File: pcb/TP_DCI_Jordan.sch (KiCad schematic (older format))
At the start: 20 parts

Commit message: Rótulo en esquemático
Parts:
- added JP?: +Led, Connector_PinHeader_2.54mm:PinHeader_1x02_P2.54mm_Vertical, symbol Jumper:Jumper_2_Open
- J?: symbol PCB_LCD-rescue:Conn_01x16_Male-copia-miConector -> TP_DCI_Jordan-rescue:Conn_01x16_Male-copia-miConector-PCB_LCD-rescue
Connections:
- wire segments 73 -> 77
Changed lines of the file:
@@
 EESchema Schematic File Version 4
-LIBS:PCB_LCD-cache
+LIBS:TP_DCI_Jordan-cache
 EELAYER 29 0
 EELAYER END
@@
 encoding utf-8
 Sheet 1 1
-Title ""
-Date ""
-Rev ""
+Title "Adaptador LCD-i2c para Displays Alfanuméricos"
+Date "2022-07-03"
+Rev "1.0"
 Comp ""
-Comment1 ""
-Comment2 ""
-Comment3 ""
-Comment4 ""
+Comment1 "Autor: Jordán Joan Emmanuel"
+Comment2 "Materia:  Diseño de Circuitos Impresos"
+Comment3 "Carrera de Especialización en Sistemas Embebidos"
+Comment4 "Facultad de Ingeniería de la Universidad de Buenos Aires"
 $EndDescr
 $Comp
@@
 $EndComp
 $Comp
-L power:GND #GND?
+L power:GND #GND0101
 U 1 1 6070C733
 P 3640 5205
-F 0 "#GND?" H 3640 4955 50  0001 C CNN
+F 0 "#GND0101" H 3640 4955 50  0001 C CNN
 F 1 "GND" H 3728 5168 50  0000 L CNN
 F 2 "" H 3640 5205 50  0001 C CNN
@@
 NoConn ~ -1100 4200
 $Comp
-L power:GND #PWR?
+L power:GND #PWR0101
 U 1 1 60881173
 P 4400 4260
-F 0 "#PWR?" H 4400 4010 50  0001 C CNN
+F 0 "#PWR0101" H 4400 4010 50  0001 C CNN
 F 1 "GND" H 4540 4215 50  0000 C CNN
 F 2 "" H 4400 4260 50  0001 C CNN
@@
 EN
 $Comp
-L power:GND #PWR?
+L power:GND #PWR0102
 U 1 1 60953F2C
 P 1255 4675
-F 0 "#PWR?" H 1255 4425 50  0001 C CNN
+F 0 "#PWR0102" H 1255 4425 50  0001 C CNN
 F 1 "GND" H 1255 4530 50  0000 C CNN
 F 2 "" H 1255 4675 50  0001 C CNN
@@
 	3140 4105 3100 4105
 $Comp
-L power:VDD #PWR?
+L power:VDD #PWR0103
 U 1 1 609BF41E
 P 5270 2535
-F 0 "#PWR?" H 5270 2385 50  0001 C CNN
+F 0 "#PWR0103" H 5270 2385 50  0001 C CNN
 F 1 "VDD" H 5175 2590 50  0000 C CNN
 F 2 "" H 5270 2535 50  0001 C CNN
@@
 	5270 2535 5270 2570
 $Comp
-L power:GND #GND?
+L power:GND #GND0102
 U 1 1 609CBD66
 P 5270 3140
-F 0 "#GND?" H 5270 2890 50  0001 C CNN
+F 0 "#GND0102" H 5270 2890 50  0001 C CNN
 F 1 "GND" H 5358 3103 50  0000 L CNN
 F 2 "" H 5270 3140 50  0001 C CNN
@@
 	3465 2780 3665 2780
 $Comp
-L power:VDD #PWR?
+L power:VDD #PWR0104
 U 1 1 60A0623E
 P 3665 2715
-F 0 "#PWR?" H 3665 2565 50  0001 C CNN
+F 0 "#PWR0104" H 3665 2565 50  0001 C CNN
 F 1 "VDD" H 3785 2735 50  0000 C CNN
 F 2 "" H 3665 2715 50  0001 C CNN
@@
 Connection ~ 2390 2395
 $Comp
-L power:GND #PWR?
+L power:GND #PWR0105
 U 1 1 60816DAF
 P 3375 3145
-F 0 "#PWR?" H 3375 2895 50  0001 C CNN
+F 0 "#PWR0105" H 3375 2895 50  0001 C CNN
 F 1 "GND" H 3510 3095 50  0000 C CNN
 F 2 "" H 3375 3145 50  0001 C CNN
@@
 $EndComp
 $Comp
-L power:VDD #PWR?
+L power:VDD #PWR0106
 U 1 1 609EC6D6
 P 3640 3735
-F 0 "#PWR?" H 3640 3585 50  0001 C CNN
+F 0 "#PWR0106" H 3640 3585 50  0001 C CNN
 F 1 "VDD" H 3515 3770 50  0000 C CNN
 F 2 "" H 3640 3735 50  0001 C CNN
@@
 VDD
 $Comp
-L power:GND #PWR?
+L power:GND #PWR0107
 U 1 1 609AE205
 P 5455 4125
-F 0 "#PWR?" H 5455 3875 50  0001 C CNN
+F 0 "#PWR0107" H 5455 3875 50  0001 C CNN
 F 1 "GND" H 5315 4115 50  0000 C CNN
 F 2 "" H 5455 4125 50  0001 C CNN
@@
 EN
 $Comp
-L power:GND #PWR?
+L power:GND #PWR0108
 U 1 1 60724D0A
 P 5475 4865
-F 0 "#PWR?" H 5475 4615 50  0001 C CNN
+F 0 "#PWR0108" H 5475 4615 50  0001 C CNN
 F 1 "GND" H 5340 4810 50  0000 C CNN
 F 2 "" H 5475 4865 50  0001 C CNN
@@
 	5585 4680 5585 4780
 Connection ~ 5585 4780
-$Comp
-L PCB_LCD-rescue:Conn_01x16_Male-copia-miConector J?
-U 1 1 60A7CF24
-P 5785 4580
-F 0 "J?" H 5760 5475 50  0000 C CNN
-F 1 "Display" H 5750 5390 50  0000 C CNN
-F 2 "miConector:Conector PinHEeader_1x16P2.54 corrido" H 5785 4580 50  0001 C CNN
-F 3 "~" H 5785 4580 50  0001 C CNN
-	1    5785 4580
-	-1   0    0    -1
-$EndComp
 $Comp
 L Connector_Generic:Conn_01x04 J?
@@
 Wire Wire Line
 	5270 3090 5270 3140
-Wire Wire Line
-	5585 4780 5585 4880
 Text Notes 5505 3575 0    50   ~ 10
 Display
@@
 	5520 2720 5755 2720
 Connection ~ 5520 2720
-Wire Wire Line
-	5585 4980 5585 4880
-Connection ~ 5585 4880
 Text Notes 1470 2470 0    50   ~ 10
 Entrada
@@
 	5535 3840 5535 4180
 $Comp
-L power:VDD #PWR?
+L power:VDD #PWR0109
 U 1 1 6099C042
 P 5535 3840
-F 0 "#PWR?" H 5535 3690 50  0001 C CNN
+F 0 "#PWR0109" H 5535 3690 50  0001 C CNN
 F 1 "VDD" H 5440 3970 50  0000 C CNN
 F 2 "" H 5535 3840 50  0001 C CNN
@@
 	2025 4605 2025 4315
 $Comp
-L power:VDD #PWR?
+L power:VDD #PWR0110
 U 1 1 62BEB29E
 P 2285 3925
-F 0 "#PWR?" H 2285 3775 50  0001 C CNN
+F 0 "#PWR0110" H 2285 3775 50  0001 C CNN
 F 1 "VDD" H 2160 3960 50  0000 C CNN
 F 2 "" H 2285 3925 50  0001 C CNN
@@
 Connection ~ 1255 4505
 $Comp
-L power:GND #GND?
+L power:GND #GND0103
 U 1 1 60987354
 P 1475 3015
-F 0 "#GND?" H 1475 2765 50  0001 C CNN
+F 0 "#GND0103" H 1475 2765 50  0001 C CNN
 F 1 "GND" H 1265 3010 50  0000 L CNN
 F 2 "" H 1475 3015 50  0001 C CNN
@@
 Text Label 2800 4105 2    50   ~ 10
 SCL
+Wire Wire Line
+	5000 5480 5030 5480
+Text Label 5000 5480 2    50   ~ 10
+Vin
+$Comp
+L Jumper:Jumper_2_Open JP?
+U 1 1 62C3BED3
+P 5230 5480
+F 0 "JP?" H 5230 5715 50  0000 C CNN
+F 1 "+Led" H 5230 5624 50  0000 C CNN
+F 2 "Connector_PinHeader_2.54mm:PinHeader_1x02_P2.54mm_Vertical" H 5230 5480 50  0001 C CNN
+F 3 "~" H 5230 5480 50  0001 C CNN
+	1    5230 5480
+	1    0    0    -1
+$EndComp
+Wire Wire Line
+	5582 5480 5430 5480
+Wire Wire Line
+	5585 4980 5585 4880
+Wire Wire Line
+	5585 4780 5585 4880
+Connection ~ 5585 4880
+$Comp
+L TP_DCI_Jordan-rescue:Conn_01x16_Male-copia-miConector-PCB_LCD-rescue J?
+U 1 1 60A7CF24
+P 5785 4580
+F 0 "J?" H 5760 5475 50  0000 C CNN
+F 1 "Display" H 5750 5390 50  0000 C CNN
+F 2 "miConector:Conector PinHEeader_1x16P2.54 corrido" H 5785 4580 50  0001 C CNN
+F 3 "~" H 5785 4580 50  0001 C CNN
+	1    5785 4580
+	-1   0    0    -1
+$EndComp
+$Comp
+L power:GND #PWR?
+U 1 1 62C42C72
+P 5512 5638
+F 0 "#PWR?" H 5512 5388 50  0001 C CNN
+F 1 "GND" H 5517 5465 50  0000 C CNN
+F 2 "" H 5512 5638 50  0001 C CNN
+F 3 "" H 5512 5638 50  0001 C CNN
+	1    5512 5638
+	1    0    0    -1
+$EndComp
+Wire Wire Line
+	5583 5580 5512 5580
+Wire Wire Line
+	5512 5580 5512 5638
+Text Notes 5816 5509 0    39   ~ 8
+A
+Text Notes 5813 5609 0    39   ~ 8
+K
 $EndSCHEMATC

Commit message: avance con esquemático
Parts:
- removed JP? (x2): +Led, Connector_PinHeader_2.54mm:PinHeader_1x02_P2.54mm_Vertical, symbol Jumper:Jumper_2_Open
- D?: value 5v6 -> 5v
- L?: value 470uH -> 47uH
- RV?: value 5K -> 10k
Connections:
- net Vin: now also J?.15 (Pin_15)
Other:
- moved on the sheet: C?, D?, J?, L?, R?, RV?, SW?, U?

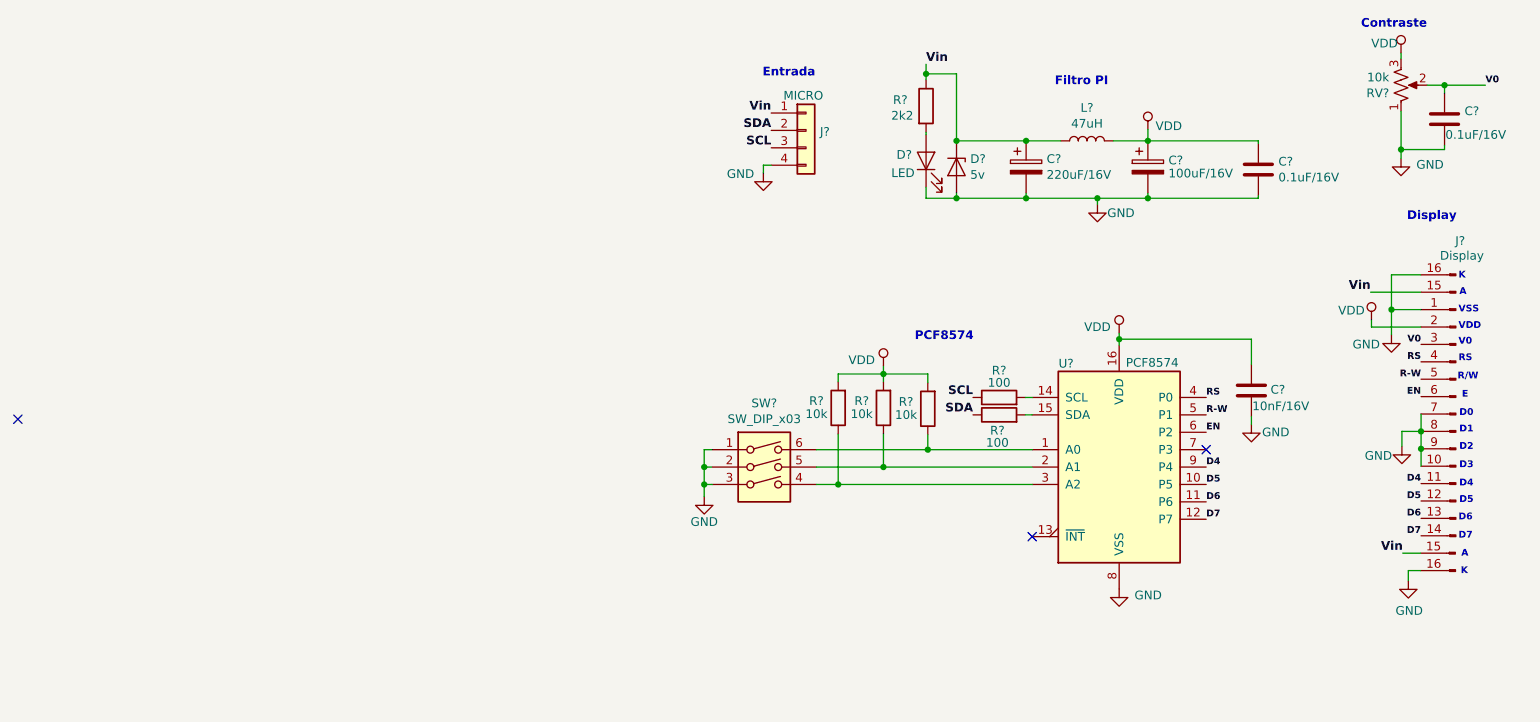
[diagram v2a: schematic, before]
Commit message: huella SMD para PCF8574 y DIPSwitch
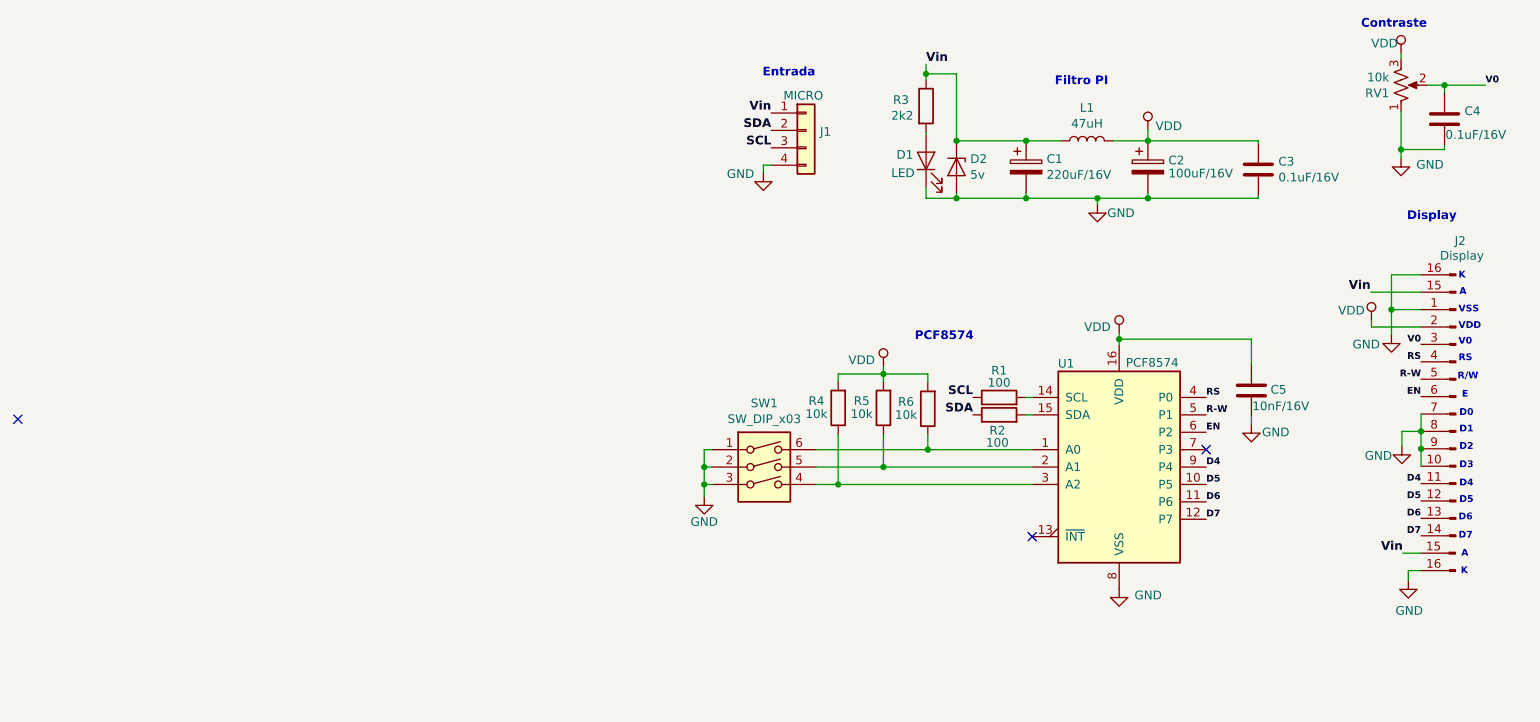
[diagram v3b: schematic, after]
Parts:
- J2: renamed from J?; footprint miConector:Conector PinHEeader_1x16P2.54 corrido -> Connector_PinHeader_2.54mm:PinHeader_1x18_P2.54mm_Vertical
- SW1: renamed from SW?; footprint (none) -> miConector:DIPSwitch_03
- U1: renamed from U?; footprint Package_DIP:DIP-16_W7.62mm_Socket_LongPads -> miSMD:SOIC127P1030X265-16N
- gave numbers to parts that had none: 16
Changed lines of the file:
@@
 $EndDescr
 $Comp
-L Device:R_POT_US RV?
+L Device:R_POT_US RV1
 U 1 1 606F83D1
 P 6850 2280
-F 0 "RV?" H 6782 2326 50  0000 R CNN
+F 0 "RV1" H 6782 2326 50  0000 R CNN
 F 1 "10k" H 6782 2235 50  0000 R CNN
 F 2 "miPotenciometro_RV09:miPote10k_3362P" H 6850 2280 50  0001 C CNN
@@
 $EndComp
 $Comp
-L Device:D_Zener D?
+L Device:D_Zener D2
 U 1 1 606FC2E1
 P 4295 2750
-F 0 "D?" V 4249 2829 50  0000 L CNN
+F 0 "D2" V 4249 2829 50  0000 L CNN
 F 1 "5v" V 4340 2829 50  0000 L CNN
 F 2 "miDiodo:miZener" H 4295 2750 50  0001 C CNN
@@
 $EndComp
 $Comp
-L Device:CP C?
+L Device:CP C1
 U 1 1 606FDAF6
 P 4695 2750
-F 0 "C?" H 4813 2796 50  0000 L CNN
+F 0 "C1" H 4813 2796 50  0000 L CNN
 F 1 "220uF/16V" H 4813 2705 50  0000 L CNN
 F 2 "miCapacitor_THT:Electrolitico_10uF" H 4733 2600 50  0001 C CNN
@@
 $EndComp
 $Comp
-L Device:C C?
+L Device:C C3
 U 1 1 60706A50
 P 6030 2765
-F 0 "C?" H 6145 2811 50  0000 L CNN
+F 0 "C3" H 6145 2811 50  0000 L CNN
 F 1 "0.1uF/16V" H 6145 2720 50  0000 L CNN
 F 2 "miCapacitor_THT:Lenteja_Ceramica" H 6068 2615 50  0001 C CNN
@@
 $EndComp
 $Comp
-L Device:LED D?
+L Device:LED D1
 U 1 1 60707A73
 P 4120 2715
-F 0 "D?" V 4155 2885 50  0000 R CNN
+F 0 "D1" V 4155 2885 50  0000 R CNN
 F 1 "LED" V 4050 2915 50  0000 R CNN
 F 2 "LED_THT:LED_D3.0mm_Clear" H 4120 2715 50  0001 C CNN
@@
 $EndComp
 $Comp
-L Device:R R?
+L Device:R R3
 U 1 1 607087CD
 P 4120 2400
-F 0 "R?" H 3930 2435 50  0000 L CNN
+F 0 "R3" H 3930 2435 50  0000 L CNN
 F 1 "2k2" H 3920 2345 50  0000 L CNN
 F 2 "Resistor_THT:R_Axial_DIN0207_L6.3mm_D2.5mm_P7.62mm_Horizontal" V 4050 2400 50  0001 C CNN
@@
 	4120 2550 4120 2565
 $Comp
-L Device:L L?
+L Device:L L1
 U 1 1 60710F6C
 P 5045 2600
-F 0 "L?" V 5235 2600 50  0000 C CNN
+F 0 "L1" V 5235 2600 50  0000 C CNN
 F 1 "47uH" V 5144 2600 50  0000 C CNN
 F 2 "Inductor_THT:L_Axial_L5.3mm_D2.2mm_P7.62mm_Horizontal_Vishay_IM-1" H 5045 2600 50  0001 C CNN
@@
 Connection ~ 4295 2600
 $Comp
-L Device:R R?
+L Device:R R2
 U 1 1 6073AF47
 P 4540 4175
-F 0 "R?" V 4450 4185 50  0000 C CNN
+F 0 "R2" V 4450 4185 50  0000 C CNN
 F 1 "100" V 4380 4185 50  0000 C CNN
 F 2 "Resistor_THT:R_Axial_DIN0207_L6.3mm_D2.5mm_P7.62mm_Horizontal" V 4470 4175 50  0001 C CNN
@@
 $EndComp
 $Comp
-L Device:R R?
+L Device:R R1
 U 1 1 6073C403
 P 4540 4075
-F 0 "R?" V 4695 4075 50  0000 C CNN
+F 0 "R1" V 4695 4075 50  0000 C CNN
 F 1 "100" V 4625 4075 50  0000 C CNN
 F 2 "Resistor_THT:R_Axial_DIN0207_L6.3mm_D2.5mm_P7.62mm_Horizontal" V 4470 4075 50  0001 C CNN
@@
 NoConn ~ 4730 4875
 $Comp
-L Device:CP C?
+L Device:CP C2
 U 1 1 60705391
 P 5395 2750
-F 0 "C?" H 5513 2788 50  0000 L CNN
+F 0 "C2" H 5513 2788 50  0000 L CNN
 F 1 "100uF/16V" H 5513 2713 50  0000 L CNN
 F 2 "miCapacitor_THT:Electrolitico_10uF" H 5433 2600 50  0001 C CNN
@@
 	6030 2600 5395 2600
 $Comp
-L Device:C C?
+L Device:C C5
 U 1 1 606C9E1F
 P 5990 4035
-F 0 "C?" H 6100 4040 50  0000 L CNN
+F 0 "C5" H 6100 4040 50  0000 L CNN
 F 1 "10nF/16V" H 5995 3945 50  0000 L CNN
 F 2 "miCapacitor_THT:Lenteja_Ceramica" H 6028 3885 50  0001 C CNN
@@
 $EndComp
 $Comp
-L Interface_Expansion:PCF8574 U?
+L Interface_Expansion:PCF8574 U1
 U 1 1 606C553F
 P 5230 4475
-F 0 "U?" H 4925 5070 50  0000 C CNN
+F 0 "U1" H 4925 5070 50  0000 C CNN
 F 1 "PCF8574" H 5420 5075 50  0000 C CNN
-F 2 "Package_DIP:DIP-16_W7.62mm_Socket_LongPads" H 5230 4475 50  0001 C CNN
+F 2 "miSMD:SOIC127P1030X265-16N" H 5230 4475 50  0001 C CNN
 F 3 "http://www.nxp.com/documents/data_sheet/PCF8574_PCF8574A.pdf" H 5230 4475 50  0001 C CNN
 	1    5230 4475
@@
 Connection ~ 6965 4270
 $Comp
-L Connector_Generic:Conn_01x04 J?
+L Connector_Generic:Conn_01x04 J1
 U 1 1 60771045
 P 3430 2540
-F 0 "J?" H 3510 2532 50  0000 L CNN
+F 0 "J1" H 3510 2532 50  0000 L CNN
 F 1 "MICRO" H 3300 2740 50  0000 L CNN
 F 2 "Connector_Phoenix_MSTB:PhoenixContact_MSTBVA_2,5_4-G_1x04_P5.00mm_Vertical" H 3430 2540 50  0001 C CNN
@@
 $EndComp
 $Comp
-L Device:C C?
+L Device:C C4
 U 1 1 609CA175
 P 7100 2475
-F 0 "C?" H 7215 2521 50  0000 L CNN
+F 0 "C4" H 7215 2521 50  0000 L CNN
 F 1 "0.1uF/16V" H 7105 2385 50  0000 L CNN
 F 2 "miCapacitor_THT:Lenteja_Ceramica" H 7138 2325 50  0001 C CNN
@@
 Vin
 $Comp
-L Switch:SW_DIP_x03 SW?
+L Switch:SW_DIP_x03 SW1
 U 1 1 62BC725B
 P 3190 4575
-F 0 "SW?" H 3190 5042 50  0000 C CNN
+F 0 "SW1" H 3190 5042 50  0000 C CNN
 F 1 "SW_DIP_x03" H 3190 4951 50  0000 C CNN
-F 2 "" H 3190 4575 50  0001 C CNN
+F 2 "miConector:DIPSwitch_03" H 3190 4575 50  0001 C CNN
 F 3 "~" H 3190 4575 50  0001 C CNN
 	1    3190 4575
@@
 $EndComp
 $Comp
-L Device:R R?
+L Device:R R6
 U 1 1 62BCA7E0
 P 4130 4140
-F 0 "R?" H 4255 4100 50  0000 C CNN
+F 0 "R6" H 4255 4100 50  0000 C CNN
 F 1 "10k" H 4255 4175 50  0000 C CNN
 F 2 "Resistor_THT:R_Axial_DIN0207_L6.3mm_D2.5mm_P7.62mm_Horizontal" V 4060 4140 50  0001 C CNN
@@
 	4130 4375 4130 4290
 $Comp
-L Device:R R?
+L Device:R R5
 U 1 1 62BE374F
 P 3875 4135
-F 0 "R?" H 4000 4095 50  0000 C CNN
+F 0 "R5" H 4000 4095 50  0000 C CNN
 F 1 "10k" H 4000 4170 50  0000 C CNN
 F 2 "Resistor_THT:R_Axial_DIN0207_L6.3mm_D2.5mm_P7.62mm_Horizontal" V 3805 4135 50  0001 C CNN
@@
 $EndComp
 $Comp
-L Device:R R?
+L Device:R R4
 U 1 1 62BE55E5
 P 3615 4135
-F 0 "R?" H 3740 4095 50  0000 C CNN
+F 0 "R4" H 3740 4095 50  0000 C CNN
 F 1 "10k" H 3740 4170 50  0000 C CNN
 F 2 "Resistor_THT:R_Axial_DIN0207_L6.3mm_D2.5mm_P7.62mm_Horizontal" V 3545 4135 50  0001 C CNN
@@
 Connection ~ 6965 4370
 $Comp
-L TP_DCI_Jordan-rescue:Conn_01x16_Male-copia-miConector-PCB_LCD-rescue J?
+L TP_DCI_Jordan-rescue:Conn_01x16_Male-copia-miConector-PCB_LCD-rescue J2
 U 1 1 60A7CF24
 P 7165 4070
-F 0 "J?" H 7140 4965 50  0000 C CNN
+F 0 "J2" H 7140 4965 50  0000 C CNN
 F 1 "Display" H 7130 4880 50  0000 C CNN
-F 2 "miConector:Conector PinHEeader_1x16P2.54 corrido" H 7165 4070 50  0001 C CNN
+F 2 "Connector_PinHeader_2.54mm:PinHeader_1x18_P2.54mm_Vertical" H 7165 4070 50  0001 C CNN
 F 3 "~" H 7165 4070 50  0001 C CNN
 	1    7165 4070
@@
 $EndComp
 $Comp
-L power:GND #PWR?
+L power:GND #PWR0107
 U 1 1 62C42C72
 P 6892 5128
-F 0 "#PWR?" H 6892 4878 50  0001 C CNN
+F 0 "#PWR0107" H 6892 4878 50  0001 C CNN
 F 1 "GND" H 6897 4955 50  0000 C CNN
 F 2 "" H 6892 5128 50  0001 C CNN
@@
 	6860 4970 6962 4970
 $Comp
-L power:GND #PWR?
+L power:GND #PWR0109
 U 1 1 62C74A5E
 P 6795 3715
-F 0 "#PWR?" H 6795 3465 50  0001 C CNN
+F 0 "#PWR0109" H 6795 3465 50  0001 C CNN
 F 1 "GND" H 6650 3660 50  0000 C CNN
 F 2 "" H 6795 3715 50  0001 C CNN
@@
 $EndComp
 $Comp
-L power:VDD #PWR?
+L power:VDD #PWR0111
 U 1 1 62C7F4AF
 P 6680 3630
-F 0 "#PWR?" H 6680 3480 50  0001 C CNN
+F 0 "#PWR0111" H 6680 3480 50  0001 C CNN
 F 1 "VDD" H 6565 3685 50  0000 C CNN
 F 2 "" H 6680 3630 50  0001 C CNN

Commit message: creación de PCB y orden de primeros elementos
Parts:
- J2: footprint Connector_PinHeader_2.54mm:PinHeader_1x18_P2.54mm_Vertical -> miConector:LCD_16x2_dosTipos
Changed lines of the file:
@@
 F 0 "J2" H 7140 4965 50  0000 C CNN
 F 1 "Display" H 7130 4880 50  0000 C CNN
-F 2 "Connector_PinHeader_2.54mm:PinHeader_1x18_P2.54mm_Vertical" H 7165 4070 50  0001 C CNN
+F 2 "miConector:LCD_16x2_dosTipos" H 7165 4070 50  0001 C CNN
 F 3 "~" H 7165 4070 50  0001 C CNN
 	1    7165 4070

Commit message: mejora de esquemático
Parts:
- C3, C4, C5: footprint miCapacitor_THT:Lenteja_Ceramica -> Capacitor_SMD:C_0805_2012Metric
- D2: value 5v -> 5v1
- R1, R2, R3, R4, R5, R6: footprint Resistor_THT:R_Axial_DIN0207_L6.3mm_D2.5mm_P7.62mm_Horizontal -> Resistor_SMD:R_0805_2012Metric
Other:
- note added: "Filtro Alimentación"
- note removed: "Filtro PI"
- moved on the sheet: C1, C2, C3, C4, C5, D1, D2, J1, J2, L1, R1, R2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
